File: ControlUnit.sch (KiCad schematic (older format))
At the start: 30 parts, among them U601 74HCT74N, U602 74HCT08N, U603 74LS153, U604 74HCT74N, U605 74HCT244N, U606 74HCT273N, U607 74HCT273N, U608 74LS161AN, U609 74HCT244N, U610 AT28C64B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

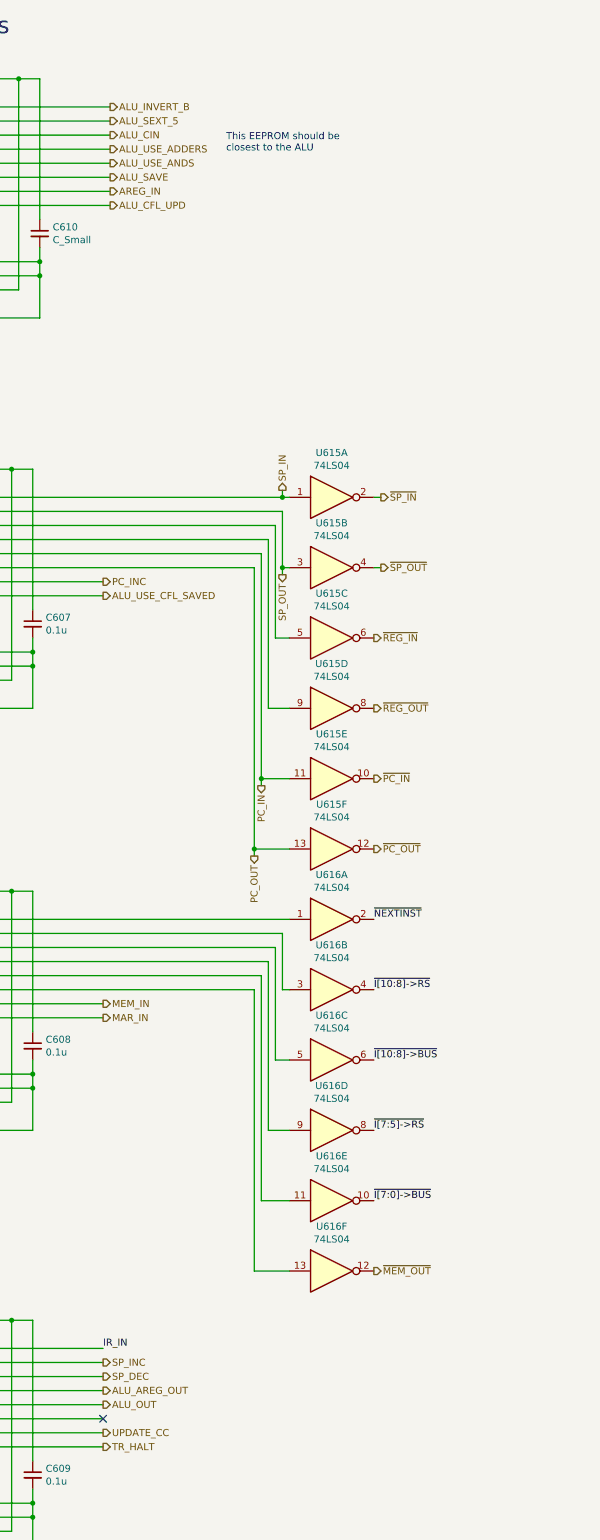
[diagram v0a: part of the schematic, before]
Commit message: Rearranged some generic logic gates in ALU to match physical net connections on the breadboard.
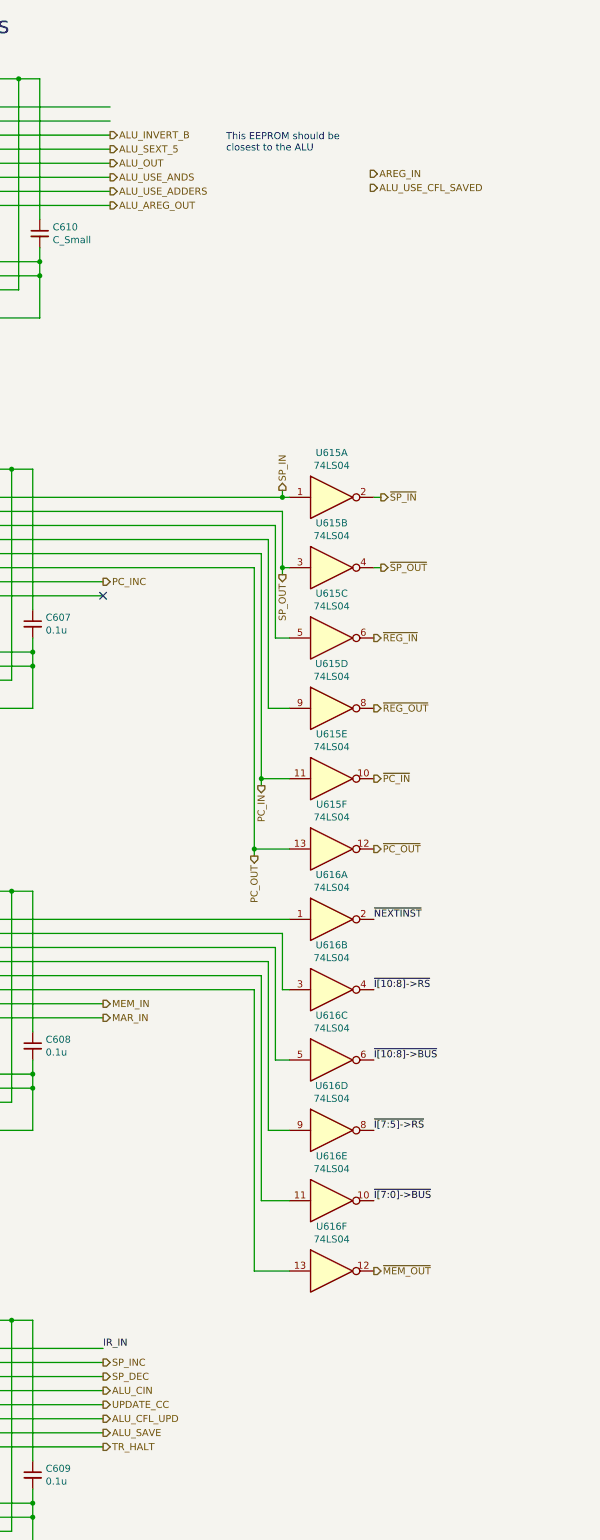
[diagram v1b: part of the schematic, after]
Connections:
- net ALU_AREG_OUT: now also U613.19 (I/O7); no longer U612.15 (I/O3)
- net ALU_CFL_UPD: now also U612.17 (I/O5); no longer U613.19 (I/O7)
- net ALU_CIN: now also U612.15 (I/O3); no longer U613.13 (I/O2)
- net ALU_INVERT_B: now also U613.13 (I/O2); no longer U613.11 (I/O0)
- net ALU_OUT: now also U613.16 (I/O4); no longer U612.16 (I/O4)
- net ALU_SAVE: now also U612.18 (I/O6); no longer U613.17 (I/O5)
- net ALU_SEXT_5: now also U613.15 (I/O3); no longer U613.12 (I/O1)
- net ALU_USE_ADDERS: now also U613.18 (I/O6); no longer U613.15 (I/O3)
- net ALU_USE_ANDS: now also U613.17 (I/O5); no longer U613.16 (I/O4)
- net ALU_USE_CFL_SAVED: no longer U610.19 (I/O7)
- net AREG_IN: no longer U613.18 (I/O6)
- net UPDATE_CC: now also U612.16 (I/O4); no longer U612.18 (I/O6)
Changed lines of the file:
@@
 Text Label 16250 10725 0    50   ~ 0
 ~NEXTINST
-Text HLabel 14375 5450 2    50   Output ~ 0
+Text HLabel 14325 14375 2    50   Output ~ 0
 ALU_SAVE
 Text HLabel 14325 11325 2    50   Output ~ 0
@@
 Text Label 14325 13775 0    50   ~ 0
 IR_IN
-Text HLabel 14375 5550 2    50   Output ~ 0
+Text HLabel 16225 5425 2    50   Output ~ 0
 AREG_IN
 Text HLabel 11275 2175 2    50   Output ~ 0
@@
 Text Label 12625 8175 2    50   ~ 0
 OPC_3
-Text HLabel 14325 14375 2    50   Output ~ 0
+Text HLabel 14325 14175 2    50   Output ~ 0
 UPDATE_CC
 Wire Wire Line
@@
 	3050 12025 3050 12875
 NoConn ~ 4600 11725
+Text HLabel 14375 5550 2    50   Output ~ 0
+ALU_USE_ADDERS
+Text HLabel 14375 5450 2    50   Output ~ 0
+ALU_USE_ANDS
+Text HLabel 14325 14075 2    50   Output ~ 0
+ALU_CIN
 Text HLabel 14375 5250 2    50   Output ~ 0
-ALU_USE_ADDERS
-Text HLabel 14375 5350 2    50   Output ~ 0
-ALU_USE_ANDS
+ALU_SEXT_5
 Text HLabel 14375 5150 2    50   Output ~ 0
-ALU_CIN
-Text HLabel 14375 5050 2    50   Output ~ 0
-ALU_SEXT_5
-Text HLabel 14375 4950 2    50   Output ~ 0
 ALU_INVERT_B
 $Comp
@@
 	1    0    0    -1
 $EndComp
-Text HLabel 14325 8425 2    50   Output ~ 0
+Text HLabel 16225 5525 2    50   Output ~ 0
 ALU_USE_CFL_SAVED
 Wire Wire Line
@@
 Text HLabel 15400 10275 3    50   Output ~ 0
 PC_OUT
-Text HLabel 14325 14175 2    50   Output ~ 0
+Text HLabel 14375 5350 2    50   Output ~ 0
 ALU_OUT
-Text HLabel 14325 14075 2    50   Output ~ 0
+Text HLabel 14375 5650 2    50   Output ~ 0
 ALU_AREG_OUT
 Wire Wire Line
@@
 Text HLabel 15600 7675 1    50   Output ~ 0
 SP_IN
-NoConn ~ 14325 14275
+NoConn ~ 14325 8425
 Text Label 3600 12525 2    50   ~ 0
 OPC_1
 Text Label 3600 12425 2    50   ~ 0
 OPC_0
-Text HLabel 14375 5650 2    50   Output ~ 0
+Text HLabel 14325 14275 2    50   Output ~ 0
 ALU_CFL_UPD
 $EndSCHEMATC
